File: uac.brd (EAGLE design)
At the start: 100 x 100 mm, 206 parts, among them U1 MCP73833-FCI/UN, U2 ADXL345, Y1 RESONATORSMD

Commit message: Connected the accelerometer adxl345
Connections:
- new net ADXL345_INT1: U$1.114, U2.8
- new net ADXL345_INT2: U$1.115, U2.9
- new net SPI1_MISO: U$1.42, U2.12
- new net SPI1_MOSI: U$1.43, U2.13
- new net SPI1_NSS: U$1.40, U2.7
- new net SPI1_SCK: U$1.41, U2.14
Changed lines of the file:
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@@
 <wire x1="68.0988" y1="6.6886" x2="73.5" y2="9.15" width="0" layer="19" extent="16-16"/>
+</signal>
+<signal name="SPI1_NSS">
+<contactref element="U$1" pad="40"/>
+<contactref element="U2" pad="7"/>
+<wire x1="-5.1" y1="3" x2="57.25" y2="39.4" width="0" layer="19" extent="1-16"/>
+</signal>
+<signal name="SPI1_SCK">
+<contactref element="U$1" pad="41"/>
+<contactref element="U2" pad="14"/>
+<wire x1="-0.9" y1="3" x2="56.75" y2="39.4" width="0" layer="19" extent="1-16"/>
+</signal>
+<signal name="SPI1_MISO">
+<contactref element="U$1" pad="42"/>
+<contactref element="U2" pad="12"/>
+<wire x1="-1.8" y1="1.9" x2="56.25" y2="39.4" width="0" layer="19" extent="1-16"/>
+</signal>
+<signal name="SPI1_MOSI">
+<contactref element="U$1" pad="43"/>
+<contactref element="U2" pad="13"/>
+<wire x1="-1" y1="1.9" x2="55.75" y2="39.4" width="0" layer="19" extent="1-16"/>
+</signal>
+<signal name="ADXL345_INT1">
+<contactref element="U$1" pad="114"/>
+<contactref element="U2" pad="8"/>
+<wire x1="-5" y1="1.9" x2="43.75" y2="60.6" width="0" layer="19" extent="1-16"/>
+</signal>
+<signal name="ADXL345_INT2">
+<contactref element="U$1" pad="115"/>
+<contactref element="U2" pad="9"/>
+<wire x1="-4.2" y1="1.9" x2="44.25" y2="60.6" width="0" layer="19" extent="1-16"/>
 </signal>
 </signals>

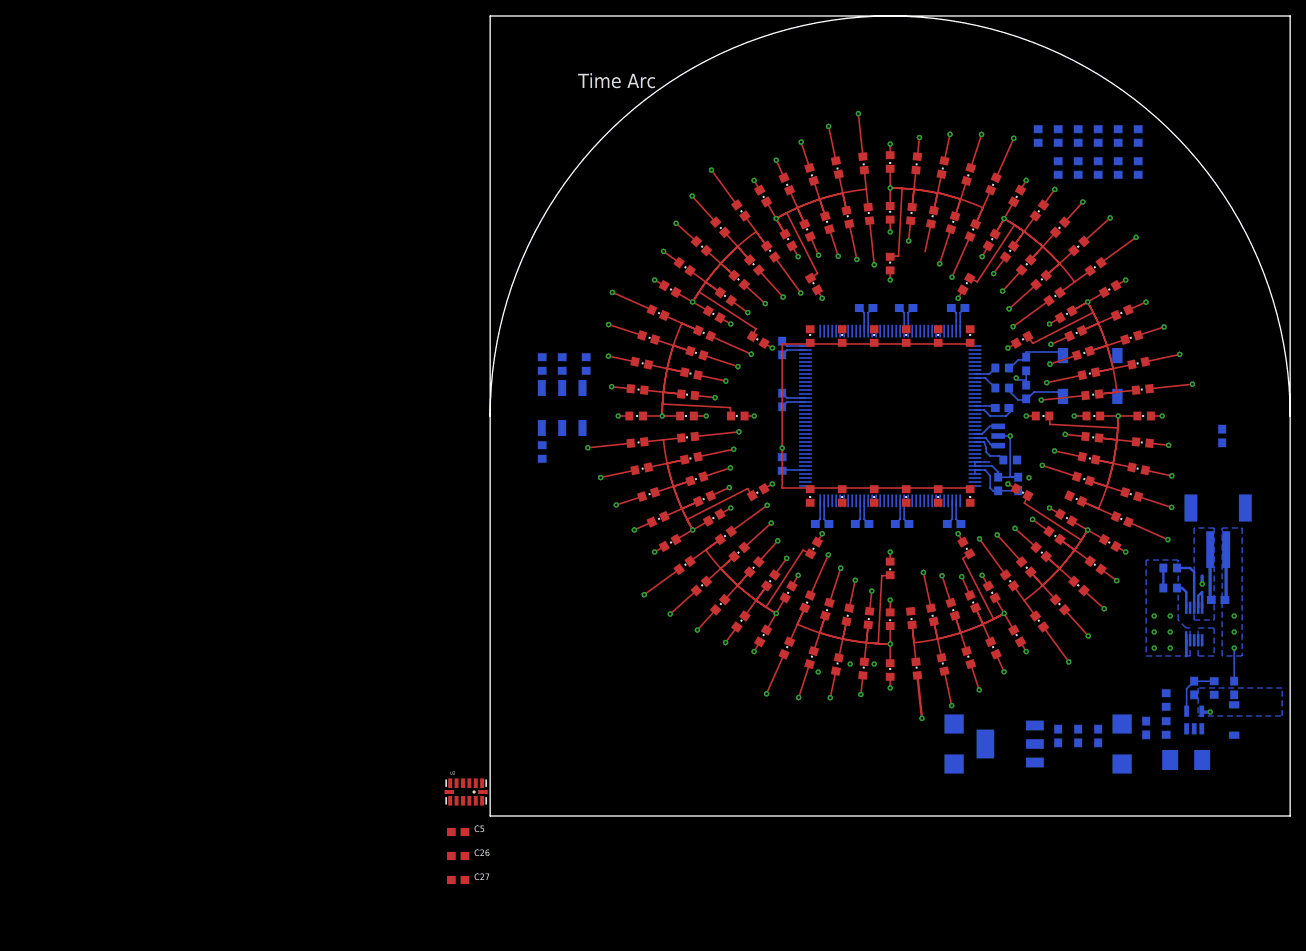
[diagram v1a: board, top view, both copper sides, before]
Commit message: Wake Up Leds 5mm
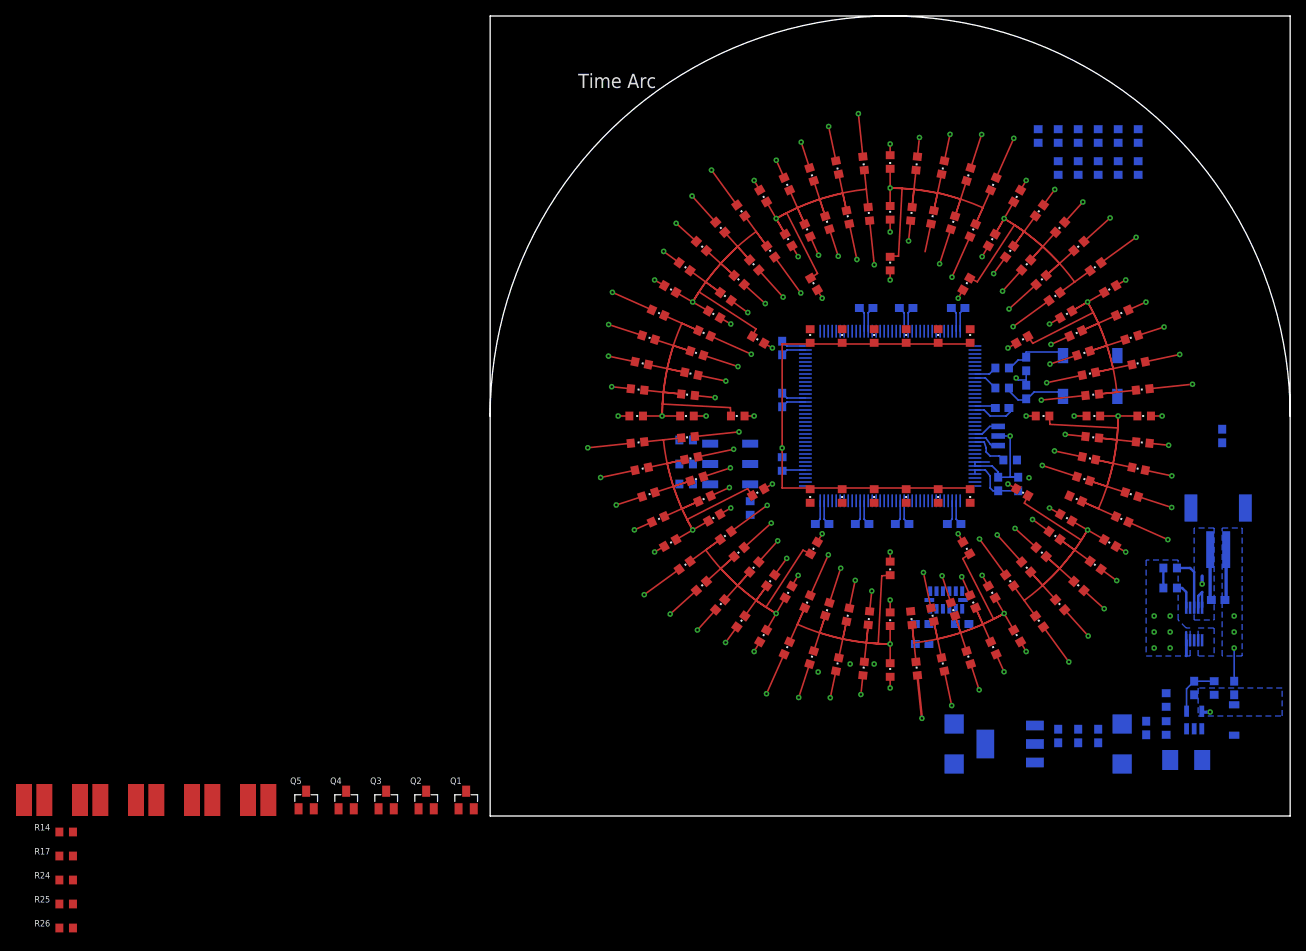
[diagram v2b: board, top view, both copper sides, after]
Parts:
- added Q1, Q2, Q3, Q4, Q5: 2N7002CK4SST, Custom components:SOT23
- added R14, R17, R24, R25, R26: 200, Custom components:R0603
- added U$4, U$5, U$6, U$7, U$8: LED_5MM_SMD, timearc:LED_5MM_SMD
- moved C27 70.7 mm to (59.0, 24.0), flipped to the bottom
- moved U2 64.6 mm to (57.0, 27.0), flipped to the bottom, turned to 180 degrees
- moved C26 63.8 mm to (54.0, 21.5), flipped to the bottom, turned to 180 degrees
- moved C5 63.6 mm to (54.0, 24.0), flipped to the bottom, turned to 180 degrees
- moved R43 26.9 mm to (32.5, 38.5)
- moved R36 23.4 mm to (24.5, 41.5), turned to 180 degrees
- moved MASTER_PROG 22.1 mm to (30.0, 44.0), turned to 270 degrees
- moved R31 19.9 mm to (24.5, 44.0), turned to 180 degrees
- moved R23 15.7 mm to (24.5, 47.0), turned to 180 degrees
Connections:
- new net N$23: Q1.3, U$4.P$2
- new net N$24: Q2.3, U$5.P$2
- new net N$25: Q3.3, U$6.P$2
- new net N$26: Q4.3, U$7.P$2
- new net N$28: Q5.3, U$8.P$2
- new net N$29: R14.1, U$4.P$1
- new net N$30: R17.1, U$5.P$1
- new net N$31: R24.1, U$6.P$1
- new net N$32: R25.1, U$7.P$1
- new net N$33: R26.1, U$8.P$1
- new net WAKE1: Q1.1
- new net WAKE2: Q2.1
- new net WAKE3: Q3.1
- new net WAKE4: Q4.1
- new net WAKE5: Q5.1
- net +5V: now also R14.2, R17.2, R24.2, R25.2, R26.2
- net ADXL345_INT1: now also U$1.46; no longer U$1.114
- net ADXL345_INT2: now also U$1.47; no longer U$1.115
- net GND: now also Q1.2, Q2.2, Q3.2, Q4.2, Q5.2

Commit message: placed wake up light
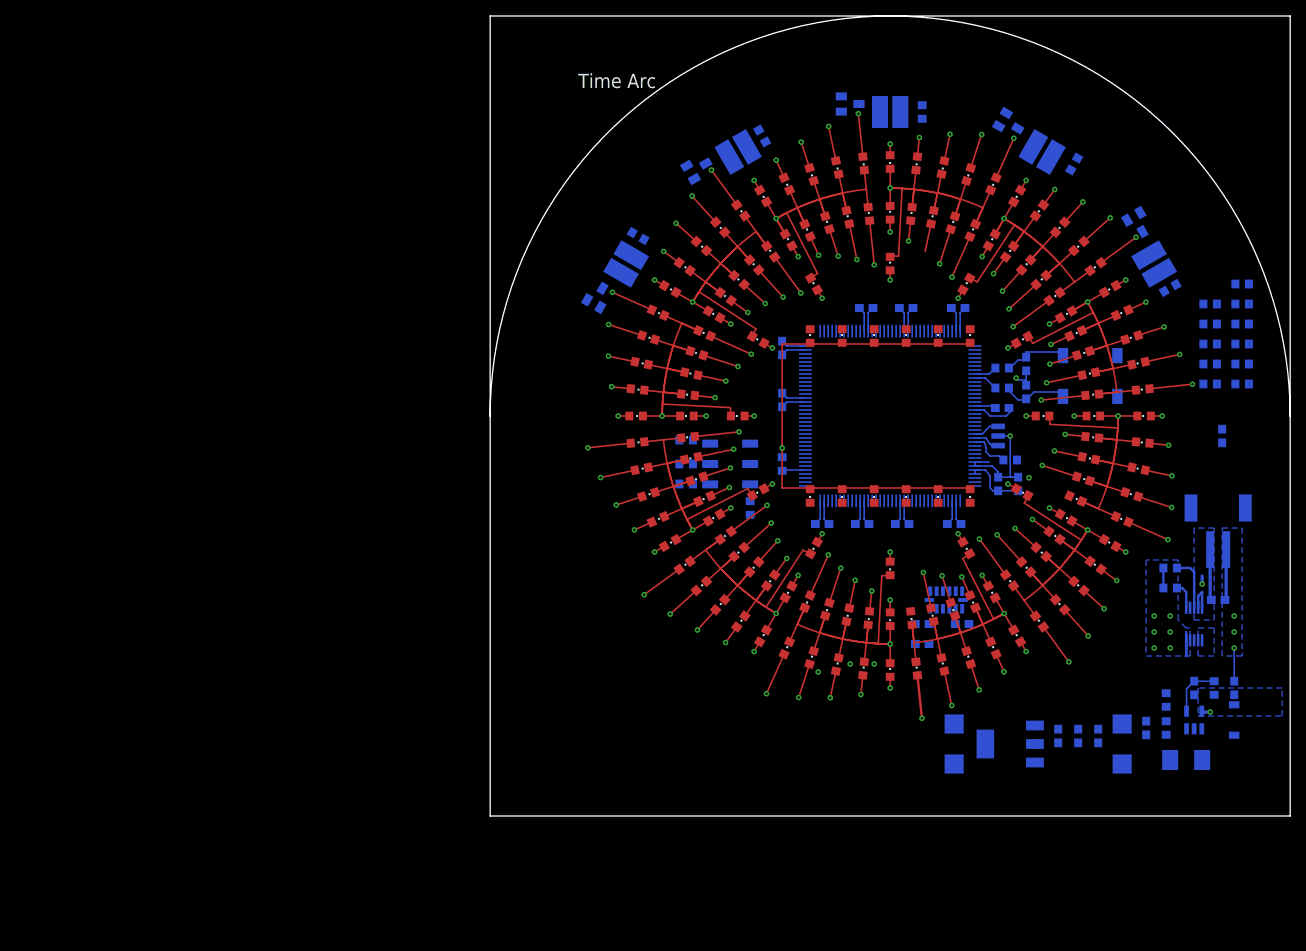
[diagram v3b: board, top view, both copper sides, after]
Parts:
- moved R26 159.5 mm to (85.0, 66.0), flipped to the bottom, turned to 150 degrees
- moved U$8 155.2 mm to (83.0, 69.0), flipped to the bottom, turned to 60 degrees
- moved R17 152.8 mm to (73.0, 81.5), flipped to the bottom, turned to 120 degrees
- moved R25 145.8 mm to (54.0, 88.0), flipped to the bottom, turned to 90 degrees
- moved U$5 132.6 mm to (69.0, 83.0), flipped to the bottom, turned to 30 degrees
- moved U$7 131.9 mm to (50.0, 88.0), flipped to the bottom
- moved R24 127.3 mm to (34.0, 85.0), flipped to the bottom, turned to 60 degrees
- moved Q5 126.5 mm to (81.0, 74.0), flipped to the bottom, turned to 150 degrees
- moved Q2 111.7 mm to (65.0, 86.5), flipped to the bottom, turned to 120 degrees
- moved U$6 109.7 mm to (31.0, 83.0), flipped to the bottom, turned to 330 degrees
- moved Q4 107.4 mm to (45.0, 89.0), flipped to the bottom, turned to 90 degrees
- moved R14 103.3 mm to (18.5, 72.5), flipped to the bottom, turned to 30 degrees
- moved Q3 88.1 mm to (26.0, 81.0), flipped to the bottom, turned to 60 degrees
- moved U$4 81.3 mm to (17.0, 69.0), flipped to the bottom, turned to 300 degrees
- moved Q1 65.1 mm to (13.5, 65.0), flipped to the bottom, turned to 30 degrees
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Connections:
- net ADXL345_INT1: now also U$1.48; no longer U$1.46
- net STAT2: now also U$1.63; no longer U$1.66
- net WAKE1: now also U$1.60
- net WAKE2: now also U$1.64
- net WAKE3: now also U$1.66
- net WAKE4: now also U$1.67
- net WAKE5: now also U$1.46

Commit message: traces
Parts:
- moved U$5 1.41 mm to (68.0, 82.0)
- moved U$8 1.21 mm to (81.9, 68.5)
- moved U$4 1.17 mm to (18.0, 68.4)
- moved U$6 1.08 mm to (31.4, 82.0)
- moved U$7 1.00 mm to (50.0, 87.0)
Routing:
- net +5V: track 0.00 -> 80.1 mm, vias 0 -> 5
- net GND: track 68.5 -> 76.3 mm, vias 14 -> 19
- net N$24: track 0.00 -> 5.39 mm
- net N$23: track 0.00 -> 5.15 mm
- net N$26: track 0.00 -> 4.92 mm
- net N$28: track 0.00 -> 4.89 mm
- net N$25: track 0.00 -> 4.75 mm
- net N$30: track 0.00 -> 3.53 mm
- net N$32: track 0.00 -> 3.31 mm
- net N$29: track 0.00 -> 3.22 mm
- net N$31: track 0.00 -> 3.06 mm
- net N$33: track 0.00 -> 2.78 mm

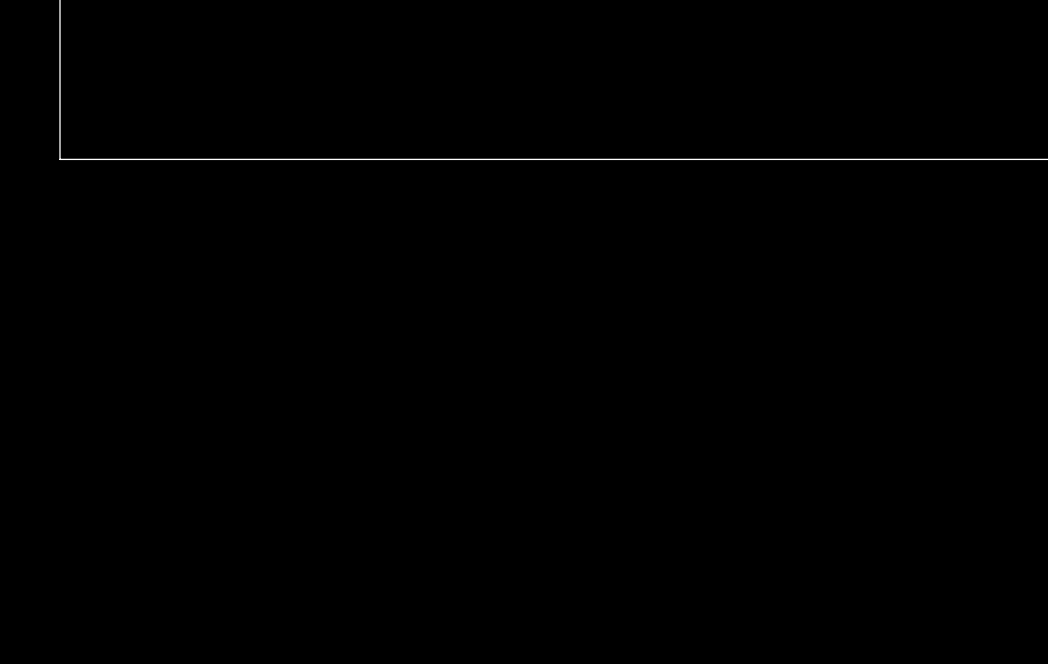
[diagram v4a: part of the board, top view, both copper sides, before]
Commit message: Added cc3000 wifi
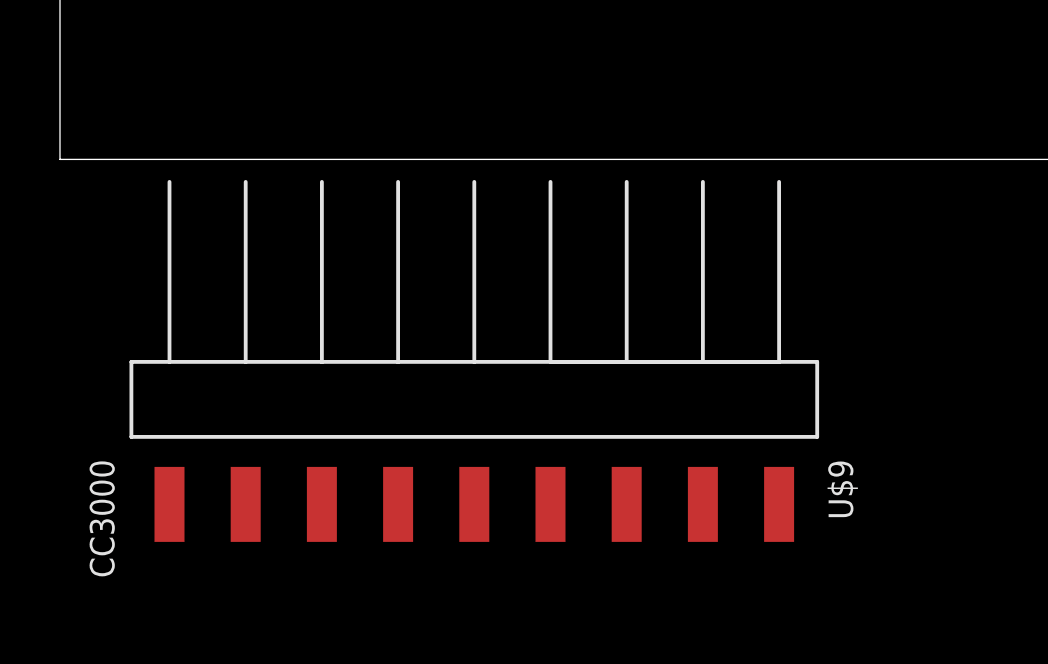
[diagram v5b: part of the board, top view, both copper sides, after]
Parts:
- added U$9: CC3000, timearc:1X09-SMD
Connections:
- net +3V3: now also U$9.1
- net GND: now also U$9.4
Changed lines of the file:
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@@
 <wire x1="4" y1="4" x2="96" y2="4" width="0.2032" layer="51"/>
 <wire x1="96" y1="4" x2="96" y2="50" width="0.2032" layer="51"/>
-<circle x="50" y="50" radius="49" width="0.2032" layer="51"/>
 </plain>
 <attributes>
@@
 <element name="U$8" library="timearc" package="LED_5MM_SMD" value="LED_5MM_SMD" x="81.9" y="68.5" rot="MR60"/>
 <element name="R26" library="Custom components" package="R0603" value="200" x="85" y="66" rot="MR150"/>
+<element name="U$9" library="timearc" package="1X09-SMD" value="CC3000" x="10" y="-8"/>
 </elements>
 <signals>
@@
 <wire x1="81.272725" y1="75.427625" x2="82.8" y2="76.3" width="0.4064" layer="16"/>
 <via x="82.8" y="76.3" extent="1-16" drill="0.31"/>
+<contactref element="U$9" pad="4"/>
 <wire x1="64.522375" y1="87.872721875" x2="81.272725" y2="75.427625" width="0" layer="19" extent="16-16"/>
 <wire x1="44" y1="90" x2="64.522375" y2="87.872721875" width="0" layer="19" extent="16-16"/>
@@
 <wire x1="88" y1="10.9" x2="88" y2="15.15" width="0" layer="19" extent="16-16"/>
 <wire x1="87.0094" y1="20.0094" x2="88" y2="15.15" width="0" layer="19" extent="16-16"/>
+<wire x1="85" y1="23" x2="87" y2="23" width="0" layer="19" extent="16-16"/>
+<wire x1="85" y1="25" x2="85" y2="23" width="0" layer="19" extent="1-1"/>
+<wire x1="85" y1="21" x2="85" y2="23" width="0" layer="19" extent="1-1"/>
+<wire x1="83" y1="25" x2="85" y2="25" width="0" layer="19" extent="1-1"/>
+<wire x1="83" y1="23" x2="85" y2="23" width="0" layer="19" extent="1-1"/>
+<wire x1="83" y1="21" x2="85" y2="21" width="0" layer="19" extent="1-1"/>
+<wire x1="84.15" y1="28.5" x2="85" y2="25" width="0" layer="19" extent="16-16"/>
 <wire x1="93" y1="16.85" x2="88" y2="15.15" width="0" layer="19" extent="16-16"/>
+<wire x1="93" y1="23" x2="93" y2="21" width="0" layer="19" extent="1-1"/>
+<wire x1="93" y1="25" x2="93" y2="23" width="0" layer="19" extent="1-1"/>
+<wire x1="92" y1="27" x2="93" y2="25" width="0" layer="19" extent="16-16"/>
 <wire x1="91.5" y1="48.35" x2="92" y2="33.3" width="0" layer="19" extent="16-16"/>
+<wire x1="8.73" y1="-11.5" x2="41" y2="18" width="0" layer="19" extent="1-1"/>
 </signal>
 <signal name="+3V3">
@@
 <contactref element="C26" pad="1"/>
 <contactref element="C5" pad="1"/>
+<contactref element="U$9" pad="1"/>
 <wire x1="65.85" y1="44.5" x2="91.5" y2="46.65" width="0" layer="19" extent="16-16"/>
 <wire x1="66" y1="40.65" x2="65.85" y2="44.5" width="0" layer="19" extent="16-16"/>
@@
 <wire x1="68.0988" y1="9" x2="61.901" y2="9" width="0" layer="19" extent="16-16"/>
 <wire x1="71" y1="9.15" x2="68.0988" y2="9" width="0" layer="19" extent="16-16"/>
+<wire x1="16.35" y1="-11.5" x2="58" y2="11.5" width="0" layer="19" extent="1-16"/>
 </signal>
 <signal name="N$1">
